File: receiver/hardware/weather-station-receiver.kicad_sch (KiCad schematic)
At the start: 11 parts, among them J1 AntennaConnector, U1 RFM69, U2 PicoW, U3 APDS-9306-065, U4 BME280

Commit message: Finished Layout
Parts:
- added C4: 10uF, Capacitor_SMD:C_0805_2012Metric_Pad1.18x1.45mm_HandSolder, symbol Device:C
- U2: footprint Weather_Station_Receiver:Pico SMD Headers -> Weather_Station_Receiver:Pico_SMD_Headers
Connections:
- net +3.3V: now also C4.1
- net GND: now also C4.2
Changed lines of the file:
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@@
 	)
 	(junction
+		(at 73.66 154.94)
+		(diameter 0)
+		(color 0 0 0 0)
+	)
+	(junction
 		(at 175.26 144.78)
 		(diameter 0)
@@
 	(wire
 		(pts
+			(xy 73.66 154.94) (xy 80.01 154.94)
+		)
+		(stroke
+			(width 0)
+			(type default)
+		)
+	)
+	(wire
+		(pts
 			(xy 167.64 134.62) (xy 175.26 134.62)
 		)
@@
 	(wire
 		(pts
+			(xy 80.01 146.05) (xy 80.01 147.32)
+		)
+		(stroke
+			(width 0)
+			(type default)
+		)
+	)
+	(wire
+		(pts
 			(xy 36.83 152.4) (xy 40.64 152.4)
 		)
@@
 	)
 	(symbol
+		(lib_id "Device:C")
+		(at 80.01 151.13 0)
+		(unit 1)
+		(exclude_from_sim no)
+		(in_bom yes)
+		(on_board yes)
+		(dnp no)
+		(fields_autoplaced yes)
+		(property "Reference" "C4"
+			(at 83.82 149.8599 0)
+			(effects
+				(font
+					(size 1.27 1.27)
+				)
+				(justify left)
+			)
+		)
+		(property "Value" "10uF"
+			(at 83.82 152.3999 0)
+			(effects
+				(font
+					(size 1.27 1.27)
+				)
+				(justify left)
+			)
+		)
+		(property "Footprint" "Capacitor_SMD:C_0805_2012Metric_Pad1.18x1.45mm_HandSolder"
+			(at 80.9752 154.94 0)
+			(effects
+				(font
+					(size 1.27 1.27)
+				)
+				(hide yes)
+			)
+		)
+		(property "Datasheet" "~"
+			(at 80.01 151.13 0)
+			(effects
+				(font
+					(size 1.27 1.27)
+				)
+				(hide yes)
+			)
+		)
+		(property "Description" "Unpolarized capacitor"
+			(at 80.01 151.13 0)
+			(effects
+				(font
+					(size 1.27 1.27)
+				)
+				(hide yes)
+			)
+		)
+		(pin "1"
+		)
+		(pin "2"
+		)
+		(instances
+			(project "weather-station-receiver"
+				(path "/01cefa3a-c55f-45c5-8efc-28dc63eb7a4f"
+					(reference "C4")
+					(unit 1)
+				)
+			)
+		)
+	)
+	(symbol
 		(lib_id "Device:R")
 		(at 67.31 93.98 0)
@@
 			)
 		)
-		(property "Footprint" "Weather_Station_Receiver:Pico SMD Headers"
+		(property "Footprint" "Weather_Station_Receiver:Pico_SMD_Headers"
 			(at 142.24 83.82 0)
 			(effects
@@
 					(unit 1)
 				)
+			)
+		)
+	)
+	(symbol
+		(lib_id "power:+3.3V")
+		(at 80.01 146.05 0)
+		(unit 1)
+		(exclude_from_sim no)
+		(in_bom yes)
+		(on_board yes)
+		(dnp no)
+		(fields_autoplaced yes)
+		(property "Reference" "#PWR020"
+			(at 80.01 149.86 0)
+			(effects
+				(font
+					(size 1.27 1.27)
+				)
+				(hide yes)
+			)
+		)
+		(property "Value" "+3.3V"
+			(at 80.01 140.97 0)
+			(effects
+				(font
+					(size 1.27 1.27)
+				)
+			)
+		)
+		(property "Footprint" ""
+			(at 80.01 146.05 0)
+			(effects
+				(font
+					(size 1.27 1.27)
+				)
+				(hide yes)
+			)
+		)
+		(property "Datasheet" ""
+			(at 80.01 146.05 0)
+			(effects
+				(font
+					(size 1.27 1.27)
+				)
+				(hide yes)
+			)
+		)
+		(property "Description" "Power symbol creates a global label with name \"+3.3V\""
+			(at 80.01 146.05 0)
+			(effects
+				(font
+					(size 1.27 1.27)
+				)
+				(hide yes)
+			)
+		)
+		(pin "1"
+		)
+		(instances
+			(project "weather-station-receiver"
+				(path "/01cefa3a-c55f-45c5-8efc-28dc63eb7a4f"
+					(reference "#PWR020")
+					(unit 1)
+				)

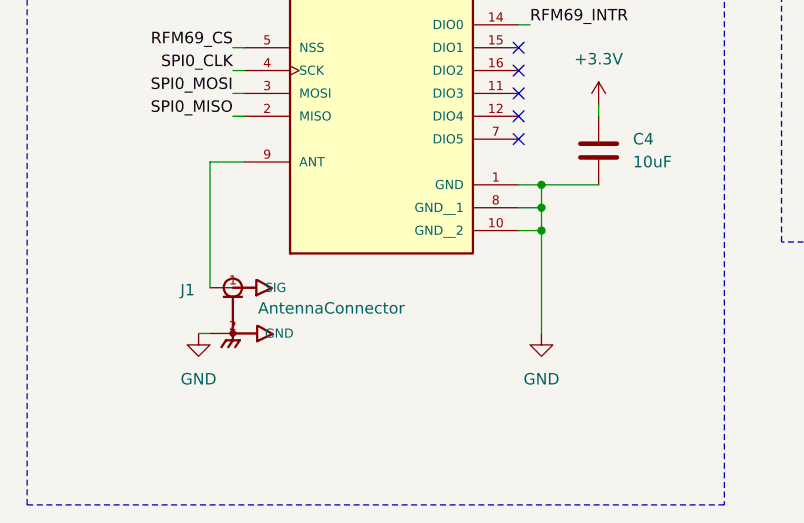
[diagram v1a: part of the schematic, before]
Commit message: Updated the weather stations components
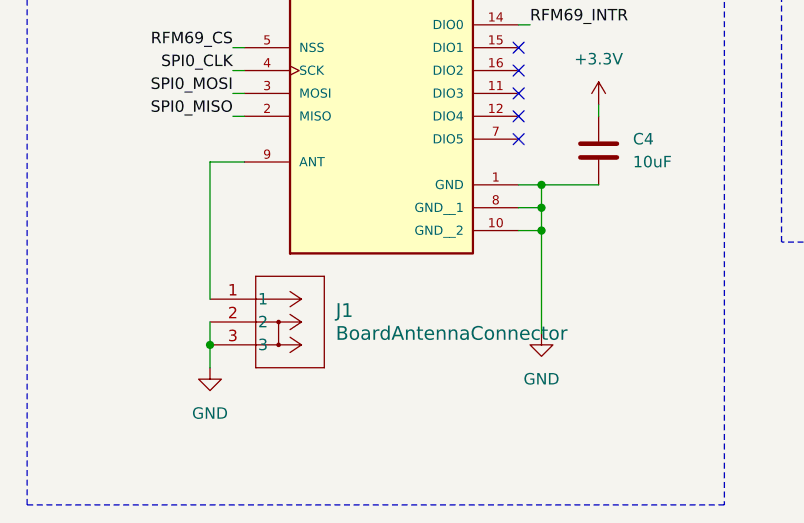
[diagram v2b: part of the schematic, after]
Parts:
- removed J1: AntennaConnector, Weather_Station_Receiver:AntennaConnector, symbol Weather_Station_Receiver:AntennaConnector
- added J1: BoardAntennaConnector, Weather_Station_Receiver:PCB_Antenna, symbol Weather_Station_Receiver:BoardAntennaConnector
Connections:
- net GND: now also J1.2, J1.3
- net at U1.9 (ANT): now also J1.1
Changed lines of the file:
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@@
 	)
 	(junction
+		(at 36.83 172.72)
+		(diameter 0)
+		(color 0 0 0 0)
+	)
+	(junction
 		(at 210.82 68.58)
 		(diameter 0)
@@
 	(wire
 		(pts
+			(xy 36.83 172.72) (xy 36.83 175.26)
+		)
+		(stroke
+			(width 0)
+			(type default)
+		)
+	)
+	(wire
+		(pts
 			(xy 167.64 78.74) (xy 168.91 78.74)
 		)
@@
 	(wire
 		(pts
-			(xy 35.56 171.45) (xy 36.83 171.45)
-		)
-		(stroke
-			(width 0)
-			(type default)
-		)
-	)
-	(wire
-		(pts
 			(xy 81.28 97.79) (xy 81.28 100.33)
 		)
@@
 	(wire
 		(pts
+			(xy 36.83 152.4) (xy 36.83 167.64)
+		)
+		(stroke
+			(width 0)
+			(type default)
+		)
+	)
+	(wire
+		(pts
 			(xy 167.64 73.66) (xy 168.91 73.66)
 		)
@@
 	(wire
 		(pts
+			(xy 36.83 170.18) (xy 36.83 172.72)
+		)
+		(stroke
+			(width 0)
+			(type default)
+		)
+	)
+	(wire
+		(pts
 			(xy 73.66 154.94) (xy 80.01 154.94)
 		)
@@
 	(wire
 		(pts
-			(xy 36.83 152.4) (xy 36.83 166.37)
-		)
-		(stroke
-			(width 0)
-			(type default)
-		)
-	)
-	(wire
-		(pts
 			(xy 167.64 149.86) (xy 175.26 149.86)
 		)
@@
 	)
 	(symbol
-		(lib_id "power:GND")
-		(at 35.56 171.45 0)
-		(unit 1)
-		(exclude_from_sim no)
-		(in_bom yes)
-		(on_board yes)
-		(dnp no)
-		(fields_autoplaced yes)
-		(property "Reference" "#PWR01"
-			(at 35.56 177.8 0)
-			(effects
-				(font
-					(size 1.27 1.27)
-				)
-				(hide yes)
-			)
-		)
-		(property "Value" "GND"
-			(at 35.56 176.53 0)
-			(effects
-				(font
-					(size 1.27 1.27)
-				)
-			)
-		)
-		(property "Footprint" ""
-			(at 35.56 171.45 0)
-			(effects
-				(font
-					(size 1.27 1.27)
-				)
-				(hide yes)
-			)
-		)
-		(property "Datasheet" ""
-			(at 35.56 171.45 0)
-			(effects
-				(font
-					(size 1.27 1.27)
-				)
-				(hide yes)
-			)
-		)
-		(property "Description" "Power symbol creates a global label with name \"GND\" , ground"
-			(at 35.56 171.45 0)
-			(effects
-				(font
-					(size 1.27 1.27)
-				)
-				(hide yes)
-			)
-		)
-		(pin "1"
-		)
-		(instances
-			(project "weather-station-receiver"
-				(path "/01cefa3a-c55f-45c5-8efc-28dc63eb7a4f"
-					(reference "#PWR01")
-					(unit 1)
-				)
-			)
-		)
-	)
-	(symbol
 		(lib_id "Weather_Station_Receiver:APDS-9306-065")
 		(at 242.57 135.89 0)
@@
 	(symbol
 		(lib_id "power:GND")
+		(at 36.83 175.26 0)
+		(unit 1)
+		(exclude_from_sim no)
+		(in_bom yes)
+		(on_board yes)
+		(dnp no)
+		(fields_autoplaced yes)
+		(property "Reference" "#PWR01"
+			(at 36.83 181.61 0)
+			(effects
+				(font
+					(size 1.27 1.27)
+				)
+				(hide yes)
+			)
+		)
+		(property "Value" "GND"
+			(at 36.83 180.34 0)
+			(effects
+				(font
+					(size 1.27 1.27)
+				)
+			)
+		)
+		(property "Footprint" ""
+			(at 36.83 175.26 0)
+			(effects
+				(font
+					(size 1.27 1.27)
+				)
+				(hide yes)
+			)
+		)
+		(property "Datasheet" ""
+			(at 36.83 175.26 0)
+			(effects
+				(font
+					(size 1.27 1.27)
+				)
+				(hide yes)
+			)
+		)
+		(property "Description" "Power symbol creates a global label with name \"GND\" , ground"
+			(at 36.83 175.26 0)
+			(effects
+				(font
+					(size 1.27 1.27)
+				)
+				(hide yes)
+			)
+		)
+		(pin "1"
+		)
+		(instances
+			(project "weather-station-receiver"
+				(path "/01cefa3a-c55f-45c5-8efc-28dc63eb7a4f"
+					(reference "#PWR01")
+					(unit 1)
+				)
+			)
+		)
+	)
+	(symbol
+		(lib_id "power:GND")
 		(at 233.68 99.06 0)
 		(unit 1)
@@
 	)
 	(symbol
+		(lib_id "Weather_Station_Receiver:BoardAntennaConnector")
+		(at 36.83 167.64 0)
+		(unit 1)
+		(exclude_from_sim no)
+		(in_bom yes)
+		(on_board yes)
+		(dnp no)
+		(fields_autoplaced yes)
+		(property "Reference" "J1"
+			(at 50.8 168.9099 0)
+			(effects
+				(font
+					(size 1.524 1.524)
+				)
+				(justify left)
+			)
+		)
+		(property "Value" "BoardAntennaConnector"
+			(at 50.8 171.4499 0)
+			(effects
+				(font
+					(size 1.524 1.524)
+				)
+				(justify left)
+			)
+		)
+		(property "Footprint" "Weather_Station_Receiver:PCB_Antenna"
+			(at 36.83 167.64 0)
+			(effects
+				(font
+					(size 1.27 1.27)
+					(italic yes)
+				)
+				(hide yes)
+			)
+		)
+		(property "Datasheet" "732511150"
+			(at 36.83 167.64 0)
+			(effects
+				(font
+					(size 1.27 1.27)
+					(italic yes)
+				)
+				(hide yes)
+			)
+		)
+		(property "Description" ""
+			(at 36.83 167.64 0)
+			(effects
+				(font
+					(size 1.27 1.27)
+				)
+				(hide yes)
+			)
+		)
+		(pin "2"
+		)
+		(pin "1"
+		)
+		(pin "3"
+		)
+		(instances
+			(project "weather-station-receiver"
+				(path "/01cefa3a-c55f-45c5-8efc-28dc63eb7a4f"
+					(reference "J1")
+					(unit 1)
+				)
+			)
+		)
+	)
+	(symbol
 		(lib_id "Weather_Station_Receiver:BME280")
 		(at 252.73 83.82 0)
@@
 					(unit 1)
 				)
-			)
-		)
-	)
-	(symbol
-		(lib_id "Weather_Station_Receiver:AntennaConnector")
-		(at 39.37 168.91 0)
-		(unit 1)
-		(exclude_from_sim no)
-		(in_bom yes)
-		(on_board yes)
-		(dnp no)
-		(property "Reference" "J1"
-			(at 33.528 166.624 0)
-			(effects
-				(font
-					(size 1.27 1.27)
-				)
-				(justify left)
-			)
-		)
-		(property "Value" "AntennaConnector"
-			(at 42.164 168.656 0)
-			(effects
-				(font
-					(size 1.27 1.27)
-				)
-				(justify left)
-			)
-		)
-		(property "Footprint" "Weather_Station_Receiver:AntennaConnector"
-			(at 39.37 168.91 0)
-			(effects
-				(font
-					(size 1.27 1.27)
-				)
-				(justify bottom)
-				(hide yes)
-			)
-		)
-		(property "Datasheet" ""
-			(at 39.37 168.91 0)
-			(effects
-				(font
-					(size 1.27 1.27)
-				)
-				(hide yes)
-			)
-		)
-		(property "Description" ""
-			(at 39.37 168.91 0)
-			(effects
-				(font
-					(size 1.27 1.27)
-				)
-				(hide yes)
-			)
-		)
-		(property "PARTREV" "B2"
-			(at 39.37 168.91 0)
-			(effects
-				(font
-					(size 1.27 1.27)
-				)
-				(justify bottom)
-				(hide yes)
-			)
-		)
-		(property "STANDARD" "Manufacturer recommendations"
-			(at 39.37 168.91 0)
-			(effects
-				(font
-					(size 1.27 1.27)
-				)
-				(justify bottom)
-				(hide yes)
-			)
-		)
-		(property "MANUFACTURER" "TE Connectivity"
-			(at 39.37 168.91 0)
-			(effects
-				(font
-					(size 1.27 1.27)
-				)
-				(justify bottom)
-				(hide yes)
-			)
-		)
-		(pin "2"
-		)
-		(pin "1"
-		)
-		(instances
-			(project "weather-station-receiver"
-				(path "/01cefa3a-c55f-45c5-8efc-28dc63eb7a4f"
-					(reference "J1")
-					(unit 1)
-				)
